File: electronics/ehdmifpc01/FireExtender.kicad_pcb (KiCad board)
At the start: 2 copper layers, 25 x 30 mm, 61 parts, among them J1 MOLEX_47151-1101, J2 CONN_15_RPI-CAM

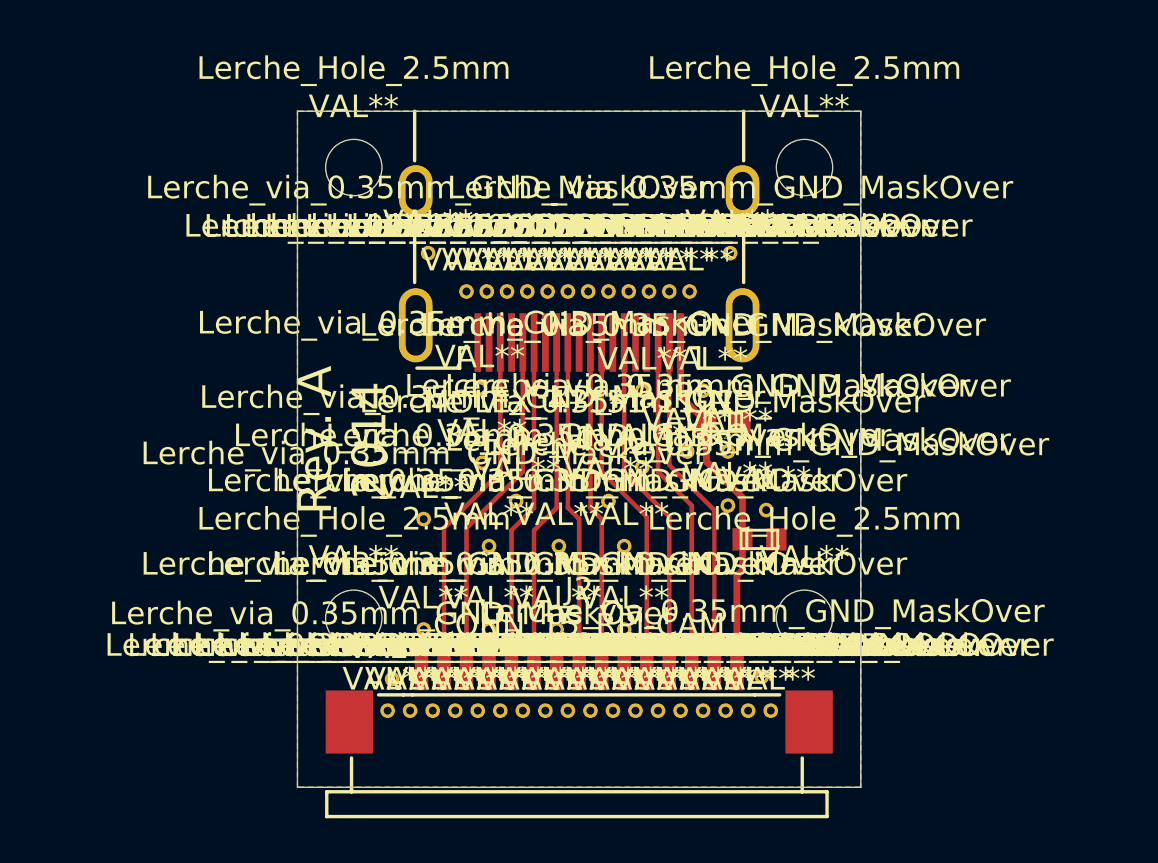
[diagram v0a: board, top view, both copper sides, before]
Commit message: Added components reference to silkscreen
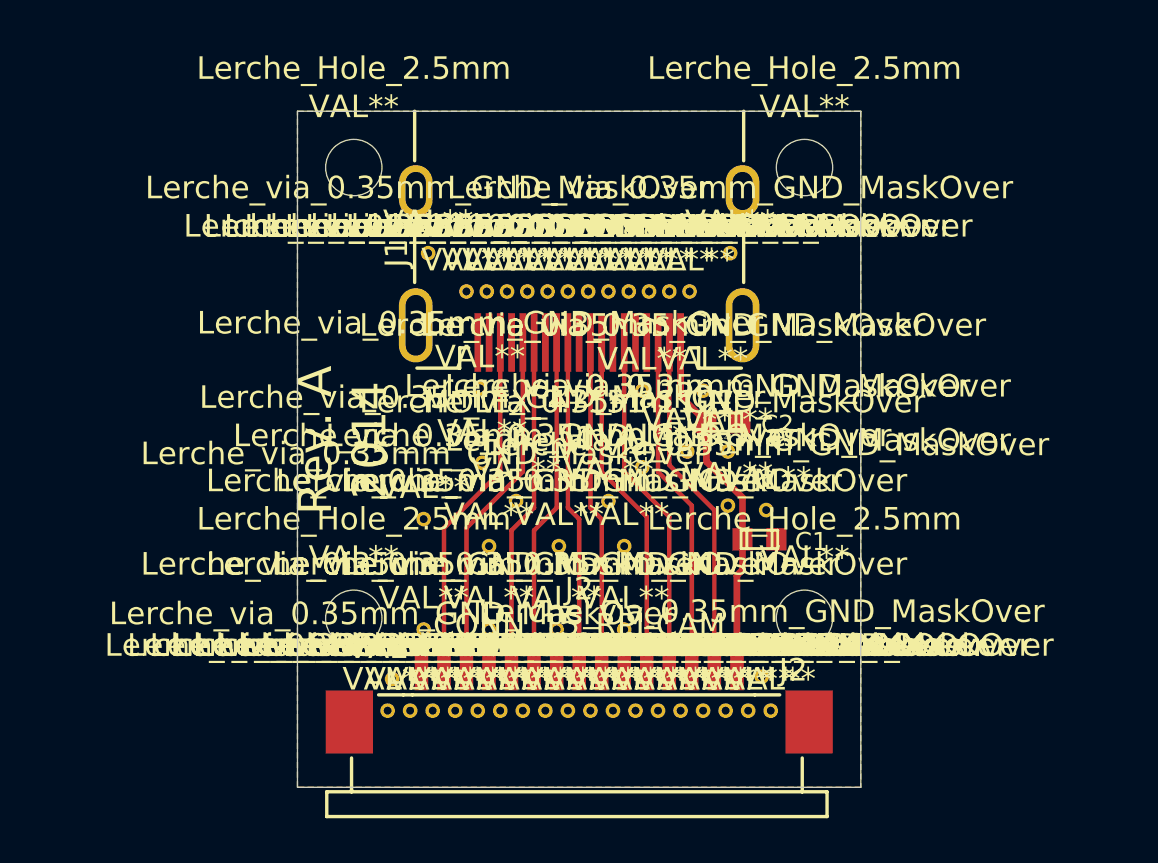
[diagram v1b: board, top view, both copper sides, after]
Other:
- board text added: "C1"
- board text added: "C2"
- board text added: "J1"
- board text added: "J2"
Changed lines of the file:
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@@
     (area 159.558334 134.225 210.841666 168.875001)
     (thickness 1.6)
-    (drawings 10)
+    (drawings 14)
     (tracks 38)
     (zones 0)
@@
     )
   )
+  (gr_text C2 (at 194 151) (layer F.SilkS)
+    (effects (font (size 0.8 0.8) (thickness 0.18)))
+  )
+  (gr_text C1 (at 195.5 156.2) (layer F.SilkS)
+    (effects (font (size 0.8 0.8) (thickness 0.18)))
+  )
+  (gr_text J2 (at 194.7 161.9) (layer F.SilkS)
+    (effects (font (size 1 1) (thickness 0.2)))
+  )
+  (gr_text J1 (at 177.1 143.4 90) (layer F.SilkS)
+    (effects (font (size 1 1) (thickness 0.2)))
+  )
   (gr_text "FirePick \nHDMI to FPC\nRev. A - 2014\nC. Lerche" (at 185.2 148.4) (layer B.SilkS)

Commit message: Differential traces are length matched now
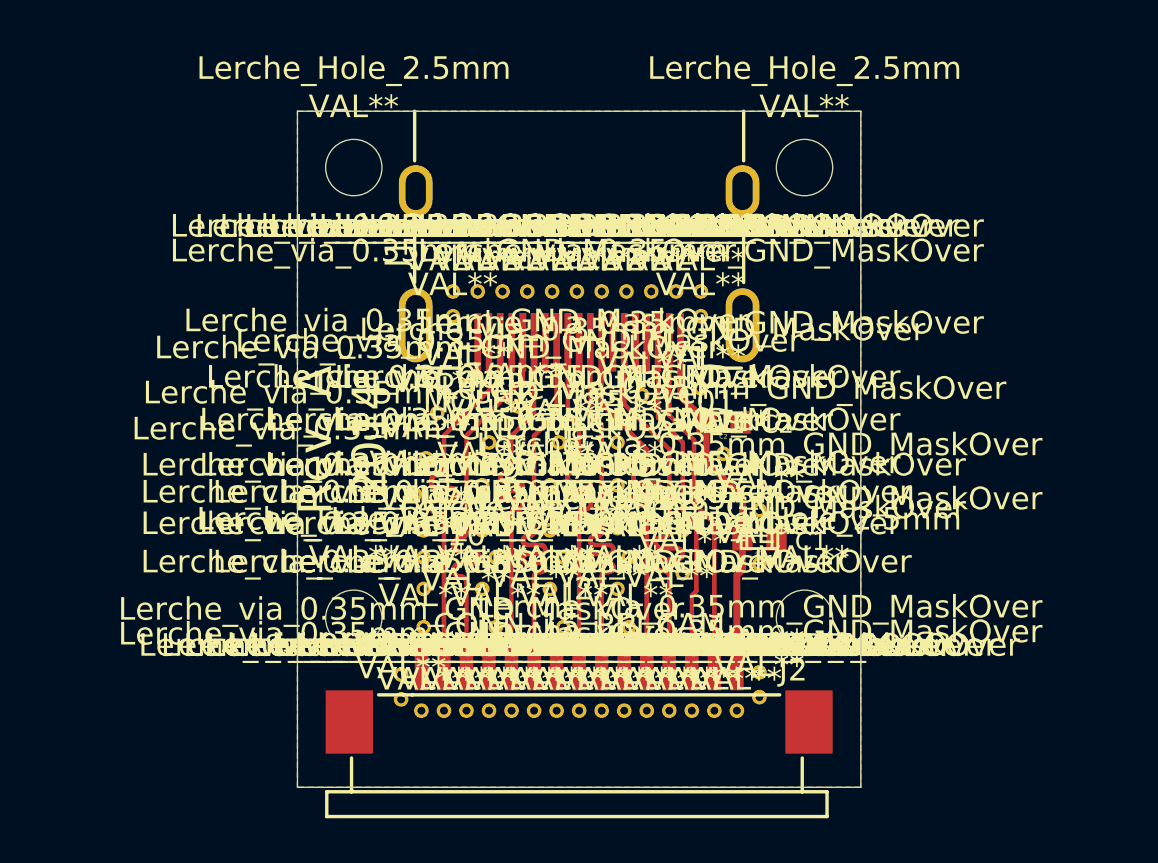
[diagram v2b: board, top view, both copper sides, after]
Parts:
- removed the Lerche_via_0.35mm_GND_MaskOver at (182.4, 154.4)
- removed the Lerche_via_0.35mm_GND_MaskOver at (180.8, 149.4)
- removed the Lerche_via_0.35mm_GND_MaskOver at (178.3, 160.1)
- removed the Lerche_via_0.35mm_GND_MaskOver at (178.5, 143.4)
- removed the Lerche_via_0.35mm_GND_MaskOver at (191.9, 143.4)
- removed the Lerche_via_0.35mm_GND_MaskOver at (179.7, 163.7)
- removed the Lerche_via_0.35mm_GND_MaskOver at (182.7, 163.7)
- removed the Lerche_via_0.35mm_GND_MaskOver at (185.7, 163.7)
- removed the Lerche_via_0.35mm_GND_MaskOver at (188.7, 163.7)
- removed the Lerche_via_0.35mm_GND_MaskOver at (191.7, 163.7)
- removed the Lerche_via_0.35mm_GND_MaskOver at (178.3, 155.2)
- removed the Lerche_via_0.35mm_GND_MaskOver at (186.5, 154.4)
- removed the Lerche_via_0.35mm_GND_MaskOver at (181.2, 156.4)
- removed the Lerche_via_0.35mm_GND_MaskOver at (184.3, 156.4)
- removed the Lerche_via_0.35mm_GND_MaskOver at (187.2, 156.4)
- removed the Lerche_via_0.35mm_GND_MaskOver at (193.5, 154.8)
- removed the Lerche_via_0.35mm_GND_MaskOver at (190.7, 149.5)
- removed the Lerche_via_0.35mm_GND_MaskOver at (191.8, 152.2)
- removed the Lerche_via_0.35mm_GND_MaskOver at (193.3, 162.2)
- removed the Lerche_via_0.35mm_GND_MaskOver at (176.9, 162.3)
- removed the Lerche_via_0.35mm_GND_MaskOver at (181.1, 145.1)
- removed the Lerche_via_0.35mm_GND_MaskOver at (182.0, 145.1)
- removed the Lerche_via_0.35mm_GND_MaskOver at (181.2, 160.1)
- removed the Lerche_via_0.35mm_GND_MaskOver at (183.8, 145.1)
- removed the Lerche_via_0.35mm_GND_MaskOver at (184.7, 145.1)
- removed the Lerche_via_0.35mm_GND_MaskOver at (185.6, 145.1)
- removed the Lerche_via_0.35mm_GND_MaskOver at (186.5, 145.1)
- removed the Lerche_via_0.35mm_GND_MaskOver at (187.4, 145.1)
- removed the Lerche_via_0.35mm_GND_MaskOver at (188.3, 145.1)
- removed the Lerche_via_0.35mm_GND_MaskOver at (189.2, 145.1)
- removed the Lerche_via_0.35mm_GND_MaskOver at (190.1, 145.1)
- removed the Lerche_via_0.35mm_GND_MaskOver at (180.2, 145.1)
- removed the Lerche_via_0.35mm_GND_MaskOver at (184.2, 160.1)
- removed the Lerche_via_0.35mm_GND_MaskOver at (181.7, 163.7)
- removed the Lerche_via_0.35mm_GND_MaskOver at (180.7, 163.7)
- removed the Lerche_via_0.35mm_GND_MaskOver at (178.7, 163.7)
- removed the Lerche_via_0.35mm_GND_MaskOver at (177.7, 163.7)
- removed the Lerche_via_0.35mm_GND_MaskOver at (183.7, 163.7)
- removed the Lerche_via_0.35mm_GND_MaskOver at (184.7, 163.7)
- removed the Lerche_via_0.35mm_GND_MaskOver at (186.7, 163.7)
- removed the Lerche_via_0.35mm_GND_MaskOver at (187.7, 163.7)
- removed the Lerche_via_0.35mm_GND_MaskOver at (189.7, 163.7)
- removed the Lerche_via_0.35mm_GND_MaskOver at (190.7, 163.7)
- removed the Lerche_via_0.35mm_GND_MaskOver at (187.2, 160.1)
- removed the Lerche_via_0.35mm_GND_MaskOver at (192.7, 163.7)
- removed the Lerche_via_0.35mm_GND_MaskOver at (193.7, 163.7)
- removed the Lerche_via_0.35mm_GND_MaskOver at (176.7, 163.7)
- removed the Lerche_via_0.35mm_GND_MaskOver at (180.9, 152.7)
- removed the Lerche_via_0.35mm_GND_MaskOver at (188.0, 149.5)
- removed the Lerche_via_0.35mm_GND_MaskOver at (188.0, 152.9)
- removed the Lerche_via_0.35mm_GND_MaskOver at (190.0, 152.2)
- removed the Lerche_via_0.35mm_GND_MaskOver at (191.8, 154.6)
- added 10: VAL**, MuSelf, F.Cu at (180.2, 158.3)
- added 11: VAL**, MuSelf, F.Cu at (189.2, 158.0)
- added 4: VAL**, MuSelf, F.Cu at (179.2, 155.5)
- added 5: VAL**, MuSelf, F.Cu at (188.2, 155.1)
- added 6: VAL**, MuSelf, F.Cu at (186.2, 158.0)
- added 7: VAL**, MuSelf, F.Cu at (185.2, 155.2)
- added 8: VAL**, MuSelf, F.Cu at (183.2, 158.0)
- added 9: VAL**, MuSelf, F.Cu at (182.2, 155.2)
- added Lerche_via_0.35mm_GND_MaskOver: VAL**, Lerche_via_0.35mm_GND_MaskOver, F.Cu at (180.7, 145.1)
- added Lerche_via_0.35mm_GND_MaskOver: VAL**, Lerche_via_0.35mm_GND_MaskOver, F.Cu at (190.6, 145.1)
- added Lerche_via_0.35mm_GND_MaskOver: VAL**, Lerche_via_0.35mm_GND_MaskOver, F.Cu at (179.6, 145.1)
- added Lerche_via_0.35mm_GND_MaskOver: VAL**, Lerche_via_0.35mm_GND_MaskOver, F.Cu at (179.6, 146.2)
- added Lerche_via_0.35mm_GND_MaskOver: VAL**, Lerche_via_0.35mm_GND_MaskOver, F.Cu at (190.6, 146.2)
- added Lerche_via_0.35mm_GND_MaskOver: VAL**, Lerche_via_0.35mm_GND_MaskOver, F.Cu at (186.9, 151.8)
- added Lerche_via_0.35mm_GND_MaskOver: VAL**, Lerche_via_0.35mm_GND_MaskOver, F.Cu at (184.3, 151.8)
- added Lerche_via_0.35mm_GND_MaskOver: VAL**, Lerche_via_0.35mm_GND_MaskOver, F.Cu at (181.2, 151.8)
- added Lerche_via_0.35mm_GND_MaskOver: VAL**, Lerche_via_0.35mm_GND_MaskOver, F.Cu at (182.5, 150.2)
- added Lerche_via_0.35mm_GND_MaskOver: VAL**, Lerche_via_0.35mm_GND_MaskOver, F.Cu at (188.0, 149.7)
- added Lerche_via_0.35mm_GND_MaskOver: VAL**, Lerche_via_0.35mm_GND_MaskOver, F.Cu at (180.2, 149.3)
- added Lerche_via_0.35mm_GND_MaskOver: VAL**, Lerche_via_0.35mm_GND_MaskOver, F.Cu at (181.8, 145.1)
- added Lerche_via_0.35mm_GND_MaskOver: VAL**, Lerche_via_0.35mm_GND_MaskOver, F.Cu at (190.6, 149.4)
- added Lerche_via_0.35mm_GND_MaskOver: VAL**, Lerche_via_0.35mm_GND_MaskOver, F.Cu at (191.6, 152.3)
- added Lerche_via_0.35mm_GND_MaskOver: VAL**, Lerche_via_0.35mm_GND_MaskOver, F.Cu at (193.2, 154.8)
- added Lerche_via_0.35mm_GND_MaskOver: VAL**, Lerche_via_0.35mm_GND_MaskOver, F.Cu at (193.2, 157.2)
- added Lerche_via_0.35mm_GND_MaskOver: VAL**, Lerche_via_0.35mm_GND_MaskOver, F.Cu at (193.2, 162.0)
- added Lerche_via_0.35mm_GND_MaskOver: VAL**, Lerche_via_0.35mm_GND_MaskOver, F.Cu at (193.2, 163.1)
- added Lerche_via_0.35mm_GND_MaskOver: VAL**, Lerche_via_0.35mm_GND_MaskOver, F.Cu at (192.2, 163.7)
- added Lerche_via_0.35mm_GND_MaskOver: VAL**, Lerche_via_0.35mm_GND_MaskOver, F.Cu at (191.2, 163.7)
- added Lerche_via_0.35mm_GND_MaskOver: VAL**, Lerche_via_0.35mm_GND_MaskOver, F.Cu at (190.2, 163.7)
- added Lerche_via_0.35mm_GND_MaskOver: VAL**, Lerche_via_0.35mm_GND_MaskOver, F.Cu at (189.2, 163.7)
- added Lerche_via_0.35mm_GND_MaskOver: VAL**, Lerche_via_0.35mm_GND_MaskOver, F.Cu at (188.2, 163.7)
- added Lerche_via_0.35mm_GND_MaskOver: VAL**, Lerche_via_0.35mm_GND_MaskOver, F.Cu at (187.2, 163.7)
- added Lerche_via_0.35mm_GND_MaskOver: VAL**, Lerche_via_0.35mm_GND_MaskOver, F.Cu at (186.2, 163.7)
- added Lerche_via_0.35mm_GND_MaskOver: VAL**, Lerche_via_0.35mm_GND_MaskOver, F.Cu at (185.2, 163.7)
- added Lerche_via_0.35mm_GND_MaskOver: VAL**, Lerche_via_0.35mm_GND_MaskOver, F.Cu at (184.2, 163.7)
- added Lerche_via_0.35mm_GND_MaskOver: VAL**, Lerche_via_0.35mm_GND_MaskOver, F.Cu at (183.2, 163.7)
- added Lerche_via_0.35mm_GND_MaskOver: VAL**, Lerche_via_0.35mm_GND_MaskOver, F.Cu at (182.2, 163.7)
- added Lerche_via_0.35mm_GND_MaskOver: VAL**, Lerche_via_0.35mm_GND_MaskOver, F.Cu at (181.2, 163.7)
- added Lerche_via_0.35mm_GND_MaskOver: VAL**, Lerche_via_0.35mm_GND_MaskOver, F.Cu at (180.2, 163.7)
- added Lerche_via_0.35mm_GND_MaskOver: VAL**, Lerche_via_0.35mm_GND_MaskOver, F.Cu at (179.2, 163.7)
- added Lerche_via_0.35mm_GND_MaskOver: VAL**, Lerche_via_0.35mm_GND_MaskOver, F.Cu at (184.0, 145.1)
- added Lerche_via_0.35mm_GND_MaskOver: VAL**, Lerche_via_0.35mm_GND_MaskOver, F.Cu at (178.2, 163.7)
- added Lerche_via_0.35mm_GND_MaskOver: VAL**, Lerche_via_0.35mm_GND_MaskOver, F.Cu at (177.3, 163.2)
- added Lerche_via_0.35mm_GND_MaskOver: VAL**, Lerche_via_0.35mm_GND_MaskOver, F.Cu at (177.3, 162.1)
- added Lerche_via_0.35mm_GND_MaskOver: VAL**, Lerche_via_0.35mm_GND_MaskOver, F.Cu at (186.9, 153.7)
- added Lerche_via_0.35mm_GND_MaskOver: VAL**, Lerche_via_0.35mm_GND_MaskOver, F.Cu at (186.9, 155.6)
- added Lerche_via_0.35mm_GND_MaskOver: VAL**, Lerche_via_0.35mm_GND_MaskOver, F.Cu at (187.4, 156.9)
- added Lerche_via_0.35mm_GND_MaskOver: VAL**, Lerche_via_0.35mm_GND_MaskOver, F.Cu at (186.9, 158.3)
- added Lerche_via_0.35mm_GND_MaskOver: VAL**, Lerche_via_0.35mm_GND_MaskOver, F.Cu at (187.4, 160.0)
- added Lerche_via_0.35mm_GND_MaskOver: VAL**, Lerche_via_0.35mm_GND_MaskOver, F.Cu at (183.9, 153.7)
- added Lerche_via_0.35mm_GND_MaskOver: VAL**, Lerche_via_0.35mm_GND_MaskOver, F.Cu at (183.9, 155.7)
- added Lerche_via_0.35mm_GND_MaskOver: VAL**, Lerche_via_0.35mm_GND_MaskOver, F.Cu at (185.1, 145.1)
- added Lerche_via_0.35mm_GND_MaskOver: VAL**, Lerche_via_0.35mm_GND_MaskOver, F.Cu at (184.5, 156.9)
- added Lerche_via_0.35mm_GND_MaskOver: VAL**, Lerche_via_0.35mm_GND_MaskOver, F.Cu at (183.9, 158.3)
- added Lerche_via_0.35mm_GND_MaskOver: VAL**, Lerche_via_0.35mm_GND_MaskOver, F.Cu at (184.5, 160.0)
- added Lerche_via_0.35mm_GND_MaskOver: VAL**, Lerche_via_0.35mm_GND_MaskOver, F.Cu at (181.5, 160.0)
- added Lerche_via_0.35mm_GND_MaskOver: VAL**, Lerche_via_0.35mm_GND_MaskOver, F.Cu at (180.9, 158.3)
- added Lerche_via_0.35mm_GND_MaskOver: VAL**, Lerche_via_0.35mm_GND_MaskOver, F.Cu at (181.5, 156.9)
- added Lerche_via_0.35mm_GND_MaskOver: VAL**, Lerche_via_0.35mm_GND_MaskOver, F.Cu at (180.9, 155.7)
- added Lerche_via_0.35mm_GND_MaskOver: VAL**, Lerche_via_0.35mm_GND_MaskOver, F.Cu at (180.9, 153.7)
- added Lerche_via_0.35mm_GND_MaskOver: VAL**, Lerche_via_0.35mm_GND_MaskOver, F.Cu at (178.3, 160.0)
- added Lerche_via_0.35mm_GND_MaskOver: VAL**, Lerche_via_0.35mm_GND_MaskOver, F.Cu at (178.3, 158.3)
- added Lerche_via_0.35mm_GND_MaskOver: VAL**, Lerche_via_0.35mm_GND_MaskOver, F.Cu at (186.2, 145.1)
- added Lerche_via_0.35mm_GND_MaskOver: VAL**, Lerche_via_0.35mm_GND_MaskOver, F.Cu at (178.3, 156.9)
- added Lerche_via_0.35mm_GND_MaskOver: VAL**, Lerche_via_0.35mm_GND_MaskOver, F.Cu at (178.3, 155.7)
- added Lerche_via_0.35mm_GND_MaskOver: VAL**, Lerche_via_0.35mm_GND_MaskOver, F.Cu at (177.9, 154.1)
- added Lerche_via_0.35mm_GND_MaskOver: VAL**, Lerche_via_0.35mm_GND_MaskOver, F.Cu at (178.4, 152.5)
- added Lerche_via_0.35mm_GND_MaskOver: VAL**, Lerche_via_0.35mm_GND_MaskOver, F.Cu at (178.9, 150.5)
- added Lerche_via_0.35mm_GND_MaskOver: VAL**, Lerche_via_0.35mm_GND_MaskOver, F.Cu at (189.8, 155.7)
- added Lerche_via_0.35mm_GND_MaskOver: VAL**, Lerche_via_0.35mm_GND_MaskOver, F.Cu at (189.8, 157.6)
- added Lerche_via_0.35mm_GND_MaskOver: VAL**, Lerche_via_0.35mm_GND_MaskOver, F.Cu at (187.3, 145.1)
- added Lerche_via_0.35mm_GND_MaskOver: VAL**, Lerche_via_0.35mm_GND_MaskOver, F.Cu at (188.4, 145.1)
- added Lerche_via_0.35mm_GND_MaskOver: VAL**, Lerche_via_0.35mm_GND_MaskOver, F.Cu at (189.5, 145.1)
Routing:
- net N-000004: track 15.5 -> 12.7 mm
- net N-0000010: track 15.5 -> 12.7 mm
- net N-000009: track 14.9 -> 12.4 mm
- net N-000008: track 14.9 -> 12.4 mm
- net N-000007: track 14.7 -> 12.2 mm
- net N-000006: track 14.7 -> 12.2 mm
- net N-000005: track 15.3 -> 12.8 mm
- net N-0000011: track 15.3 -> 12.8 mm

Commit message: Changed to correct pinout for Type A HDMI
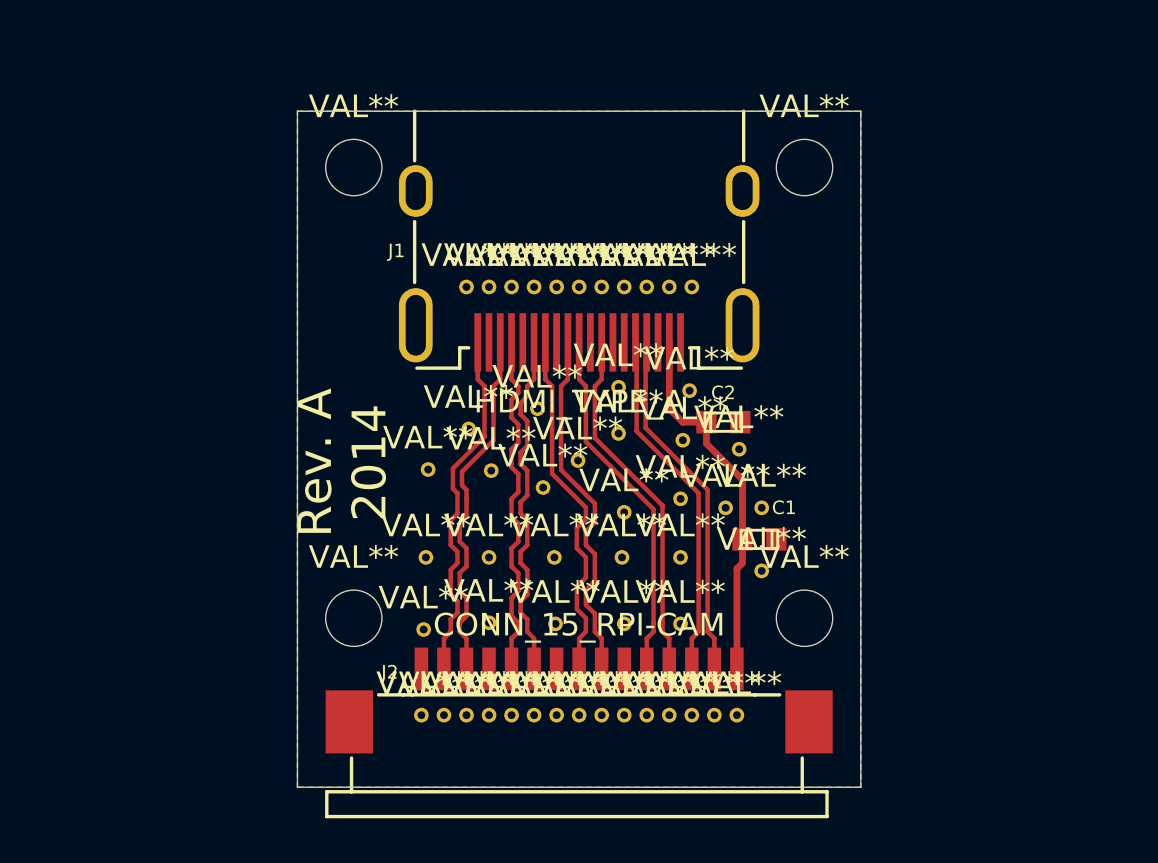
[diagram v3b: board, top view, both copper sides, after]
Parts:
- removed 10, 11, 4, 5, 6, 7, 8, 9: VAL**, MuSelf
- removed Lerche_Hole_2.5mm (x4): VAL**, Lerche_Hole_2.5mm
- removed Lerche_via_0.35mm_GND_MaskOver (x66): VAL**, Lerche_via_0.35mm_GND_MaskOver
- added ?: VAL**, Lerche_via_0.35mm_GND_MaskOver, F.Cu at (183.3, 150.3)
- added ?: VAL**, Lerche_via_0.35mm_GND_MaskOver, F.Cu at (184.2, 159.8)
- added ?: VAL**, Lerche_via_0.35mm_GND_MaskOver, F.Cu at (181.2, 159.8)
- added ?: VAL**, Lerche_Hole_2.5mm, F.Cu at (175.2, 159.6)
- added ?: VAL**, Lerche_Hole_2.5mm, F.Cu at (195.2, 159.6)
- added ?: VAL**, Lerche_Hole_2.5mm, F.Cu at (195.2, 139.6)
- added ?: VAL**, Lerche_Hole_2.5mm, F.Cu at (175.2, 139.6)
- added ?: VAL**, Lerche_via_0.35mm_GND_MaskOver, F.Cu at (189.8, 151.7)
- added ?: VAL**, Lerche_via_0.35mm_GND_MaskOver, F.Cu at (192.3, 152.1)
- added ?: VAL**, Lerche_via_0.35mm_GND_MaskOver, F.Cu at (190.1, 149.5)
- added ?: VAL**, Lerche_via_0.35mm_GND_MaskOver, F.Cu at (193.3, 154.7)
- added ?: VAL**, Lerche_via_0.35mm_GND_MaskOver, F.Cu at (181.3, 153.1)
- added ?: VAL**, Lerche_via_0.35mm_GND_MaskOver, F.Cu at (191.7, 154.7)
- added ?: VAL**, Lerche_via_0.35mm_GND_MaskOver, F.Cu at (193.3, 157.5)
- added ?: VAL**, Lerche_via_0.35mm_GND_MaskOver, F.Cu at (180.2, 144.9)
- added ?: VAL**, Lerche_via_0.35mm_GND_MaskOver, F.Cu at (181.2, 144.9)
- added ?: VAL**, Lerche_via_0.35mm_GND_MaskOver, F.Cu at (182.2, 144.9)
- added ?: VAL**, Lerche_via_0.35mm_GND_MaskOver, F.Cu at (183.2, 144.9)
- added ?: VAL**, Lerche_via_0.35mm_GND_MaskOver, F.Cu at (184.2, 144.9)
- added ?: VAL**, Lerche_via_0.35mm_GND_MaskOver, F.Cu at (185.2, 144.9)
- added ?: VAL**, Lerche_via_0.35mm_GND_MaskOver, F.Cu at (186.2, 144.9)
- added ?: VAL**, Lerche_via_0.35mm_GND_MaskOver, F.Cu at (187.2, 144.9)
- added ?: VAL**, Lerche_via_0.35mm_GND_MaskOver, F.Cu at (185.2, 152.6)
- added ?: VAL**, Lerche_via_0.35mm_GND_MaskOver, F.Cu at (188.2, 144.9)
- added ?: VAL**, Lerche_via_0.35mm_GND_MaskOver, F.Cu at (189.2, 144.9)
- added ?: VAL**, Lerche_via_0.35mm_GND_MaskOver, F.Cu at (190.2, 144.9)
- added ?: VAL**, Lerche_via_0.35mm_GND_MaskOver, F.Cu at (178.2, 163.9)
- added ?: VAL**, Lerche_via_0.35mm_GND_MaskOver, F.Cu at (179.2, 163.9)
- added ?: VAL**, Lerche_via_0.35mm_GND_MaskOver, F.Cu at (180.2, 163.9)
- added ?: VAL**, Lerche_via_0.35mm_GND_MaskOver, F.Cu at (181.2, 163.9)
- added ?: VAL**, Lerche_via_0.35mm_GND_MaskOver, F.Cu at (182.2, 163.9)
- added ?: VAL**, Lerche_via_0.35mm_GND_MaskOver, F.Cu at (183.2, 163.9)
- added ?: VAL**, Lerche_via_0.35mm_GND_MaskOver, F.Cu at (184.2, 163.9)
- added ?: VAL**, Lerche_via_0.35mm_GND_MaskOver, F.Cu at (186.9, 149.3)
- added ?: VAL**, Lerche_via_0.35mm_GND_MaskOver, F.Cu at (185.2, 163.9)
- added ?: VAL**, Lerche_via_0.35mm_GND_MaskOver, F.Cu at (186.2, 163.9)
- added ?: VAL**, Lerche_via_0.35mm_GND_MaskOver, F.Cu at (187.2, 163.9)
- added ?: VAL**, Lerche_via_0.35mm_GND_MaskOver, F.Cu at (188.2, 163.9)
- added ?: VAL**, Lerche_via_0.35mm_GND_MaskOver, F.Cu at (189.2, 163.9)
- added ?: VAL**, Lerche_via_0.35mm_GND_MaskOver, F.Cu at (190.2, 163.9)
- added ?: VAL**, Lerche_via_0.35mm_GND_MaskOver, F.Cu at (191.2, 163.9)
- added ?: VAL**, Lerche_via_0.35mm_GND_MaskOver, F.Cu at (192.2, 163.9)
- added ?: VAL**, Lerche_via_0.35mm_GND_MaskOver, F.Cu at (181.2, 156.9)
- added ?: VAL**, Lerche_via_0.35mm_GND_MaskOver, F.Cu at (184.1, 156.9)
- added ?: VAL**, Lerche_via_0.35mm_GND_MaskOver, F.Cu at (189.7, 159.8)
- added ?: VAL**, Lerche_via_0.35mm_GND_MaskOver, F.Cu at (187.1, 156.9)
- added ?: VAL**, Lerche_via_0.35mm_GND_MaskOver, F.Cu at (189.7, 156.9)
- added ?: VAL**, Lerche_via_0.35mm_GND_MaskOver, F.Cu at (183.6, 153.8)
- added ?: VAL**, Lerche_via_0.35mm_GND_MaskOver, F.Cu at (180.3, 151.2)
- added ?: VAL**, Lerche_via_0.35mm_GND_MaskOver, F.Cu at (178.3, 160.1)
- added ?: VAL**, Lerche_via_0.35mm_GND_MaskOver, F.Cu at (178.5, 153.0)
- added ?: VAL**, Lerche_via_0.35mm_GND_MaskOver, F.Cu at (178.4, 156.9)
- added ?: VAL**, Lerche_via_0.35mm_GND_MaskOver, F.Cu at (187.2, 159.8)
- added ?: VAL**, Lerche_via_0.35mm_GND_MaskOver, F.Cu at (189.7, 154.3)
- added ?: VAL**, Lerche_via_0.35mm_GND_MaskOver, F.Cu at (187.2, 154.9)
- added ?: VAL**, Lerche_via_0.35mm_GND_MaskOver, F.Cu at (186.9, 151.4)
- J1: value MOLEX_47151-1101 -> HDMI_TYPE_A
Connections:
- C1 pad 1: N-000003 -> /+3V3
- C2 pad 1: N-000003 -> /+3V3
- J1 pad 1: (no net) -> /D2+
- J1 pad 10: GND -> /CLK+
- J1 pad 11: N-000006 -> GND
- J1 pad 12: N-000005 -> /CLK-
- J1 pad 13: GND -> (no net)
- J1 pad 14: N-0000011 -> (no net)
- J1 pad 15: (no net) -> /SCL
- J1 pad 16: GND -> /SDA
- J1 pad 17: N-000001 -> GND
- J1 pad 18: N-000002 -> /+3V3
- J1 pad 19: N-000003 -> (no net)
- J1 pad 2: (no net) -> GND
- J1 pad 3: N-000004 -> /D2-
- J1 pad 4: GND -> /D1+
- J1 pad 5: N-0000010 -> GND
- J1 pad 6: N-000009 -> /D1-
- J1 pad 7: GND -> /D0+
- J1 pad 8: N-000008 -> GND
- J1 pad 9: N-000007 -> /D0-
- J2 pad 11: N-000005 -> /CLK+
- J2 pad 12: N-0000011 -> /CLK-
- J2 pad 13: N-000001 -> /SCL
- J2 pad 14: N-000002 -> /SDA
- J2 pad 15: N-000003 -> /+3V3
- J2 pad 2: N-000004 -> /D2+
- J2 pad 3: N-0000010 -> /D2-
- J2 pad 5: N-000009 -> /D1+
- J2 pad 6: N-000008 -> /D1-
- J2 pad 8: N-000007 -> /D0+
- J2 pad 9: N-000006 -> /D0-
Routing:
- net /+3V3: track 0.00 -> 16.6 mm
- net /D2+: track 0.00 -> 16.0 mm
- net /D0+: track 0.00 -> 16.0 mm
- net /D0-: track 0.00 -> 16.0 mm
- net /D2-: track 0.00 -> 16.0 mm
- net /CLK-: track 0.00 -> 16.0 mm
- net /D1+: track 0.00 -> 16.0 mm
- net /D1-: track 0.00 -> 16.0 mm
- net /CLK+: track 0.00 -> 16.0 mm
- net /SCL: track 0.00 -> 15.8 mm
- net /SDA: track 0.00 -> 15.8 mm
- net N-000003: track 15.7 -> 0.00 mm
- net N-000002: track 15.3 -> 0.00 mm
- net N-000001: track 15.3 -> 0.00 mm
- net N-000005: track 12.8 -> 0.00 mm
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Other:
- board text removed: "C1"
- board text removed: "C2"
- board text removed: "J1"
- board text removed: "J2"
